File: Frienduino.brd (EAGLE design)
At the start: 69.6 x 54.4 mm, 31 parts, among them IC1 ATMEGA328, IC2 PIC16F1454, Q2 16MHz

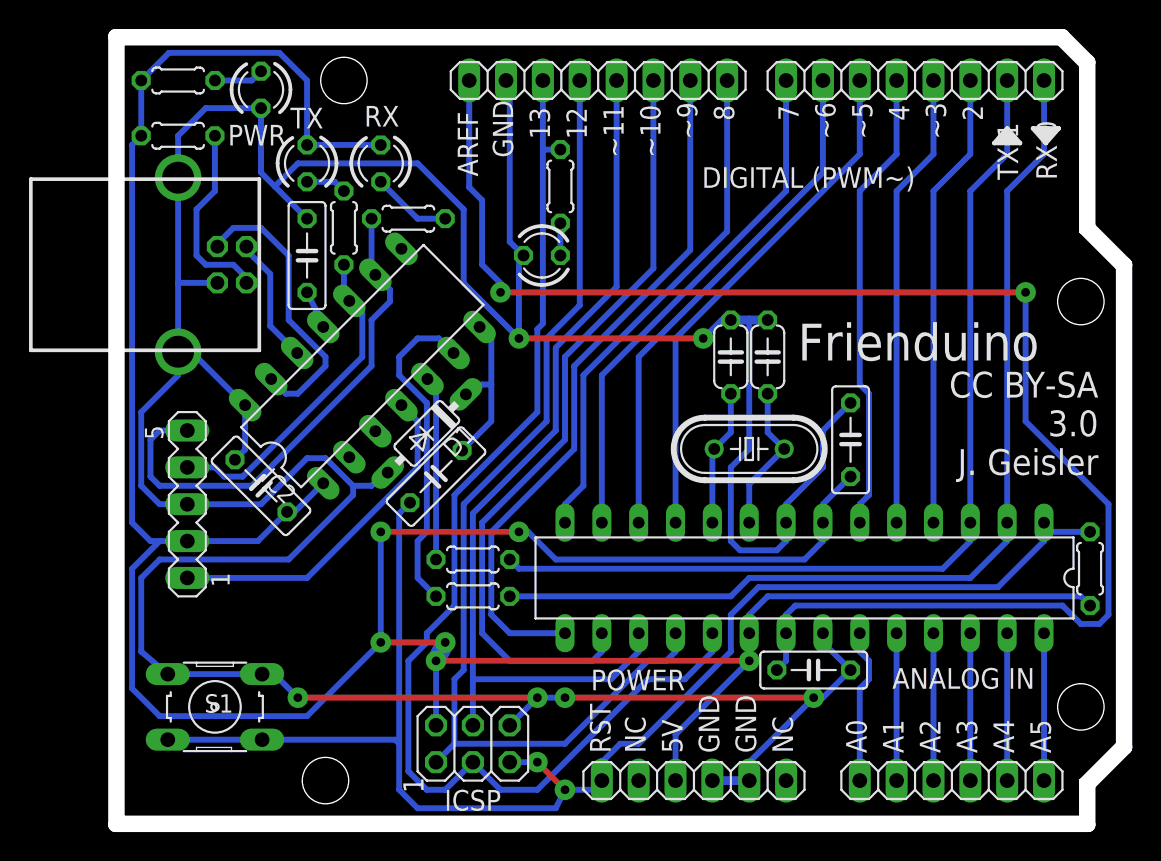
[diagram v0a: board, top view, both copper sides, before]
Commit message: changed resistors to 7mm raster
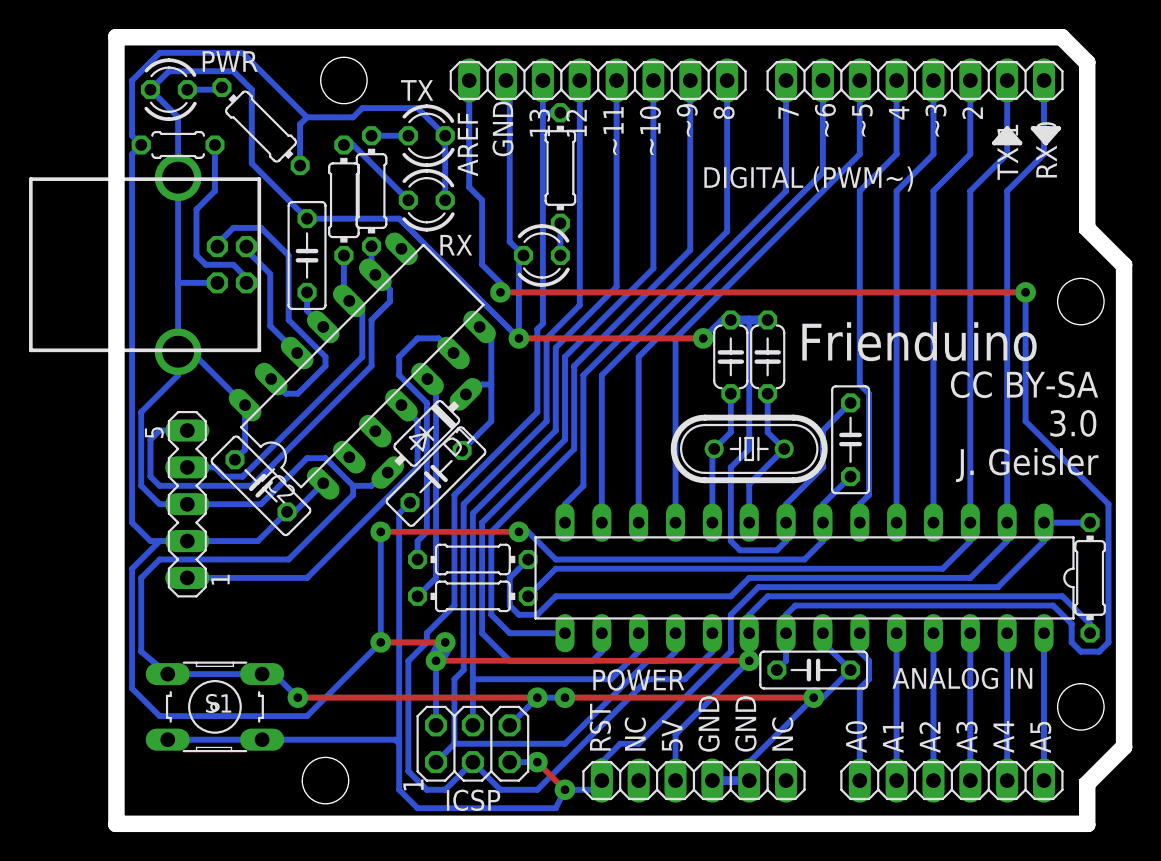
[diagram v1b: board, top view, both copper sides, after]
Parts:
- R1, R4, R5, R6, R7, R8, R9: device rcl:0204/5 -> resistor:0204/7
- moved RX 8.64 mm to (21.0, 42.5), turned to 180 degrees
- moved R6 6.54 mm to (9.53, 47.6), turned to 135 degrees
- moved PWR 6.35 mm to (3.17, 50.2), turned to 180 degrees
- moved TX 3.70 mm to (21.0, 47.0), turned to 180 degrees
- moved R4 3.18 mm to (17.1, 43.2), turned to 90 degrees
- moved R8 2.54 mm to (24.1, 17.8)
- moved R9 2.54 mm to (24.1, 15.2)
- moved R5 1.91 mm to (15.2, 42.5)
- moved R7 1.27 mm to (30.2, 44.8)
- moved F1 0.64 mm to (3.81, 46.4)
- moved R1 0.63 mm to (66.7, 16.5)
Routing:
- net +5V: track 214.0 -> 226.1 mm
- net PD0: track 68.7 -> 73.2 mm
- net AREF: track 103.6 -> 107.1 mm
- net N$9: track 2.80 -> 6.02 mm
- net M8RXD: track 22.8 -> 19.7 mm
- net M8TXD: track 12.7 -> 15.7 mm
- net N$4: track 5.50 -> 2.54 mm
- net PIC_PROG_CLK: track 35.5 -> 33.6 mm
- net N$3: track 3.44 -> 2.45 mm
- net PD1: track 65.6 -> 64.9 mm
- net N$8: track 13.2 -> 12.6 mm
- net PIC_PROG_DATA: track 22.6 -> 23.3 mm

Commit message: prepared board for manufacture and added gergers
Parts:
- ICSP: value (none) -> ISP
- SV1: value (none) -> PIC ICSP
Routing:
- net +5V: track 226.1 -> 227.5 mm
- added copper zone on layer 1, net GND
- added copper zone on layer 16, net GND
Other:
- board text added: "https://github.com/jgeisler0303/Frienduino"
- board text added: "open hardware"
- board text removed: "CC BY-SA 3.0 J. Geisler"
